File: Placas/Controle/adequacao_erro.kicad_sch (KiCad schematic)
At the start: 5 parts, among them U12 H11L1

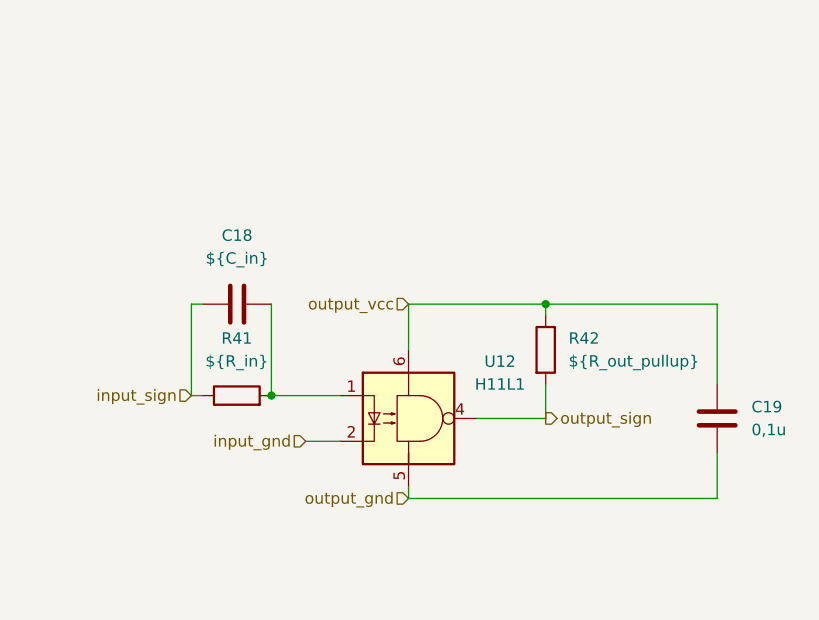
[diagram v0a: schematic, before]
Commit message: Adição de circuitos opcionais para PWM
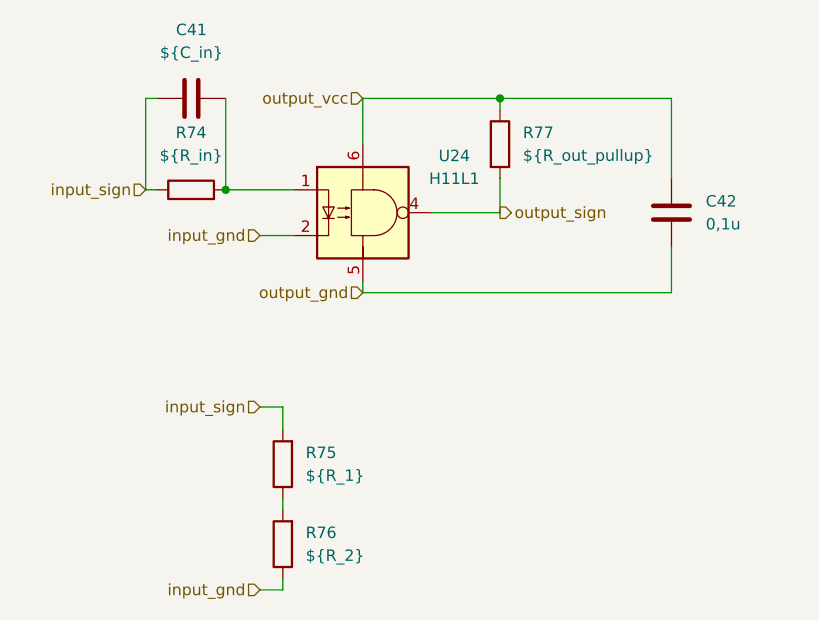
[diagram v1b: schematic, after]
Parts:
- removed C18: ${C_in}, Capacitor_THT:C_Disc_D8.0mm_W5.0mm_P7.50mm, symbol Device:C
- removed C19: 0,1u, Capacitor_THT:C_Disc_D8.0mm_W5.0mm_P7.50mm, symbol Device:C
- removed R41: ${R_in}, Resistor_THT:R_Axial_DIN0207_L6.3mm_D2.5mm_P7.62mm_Horizontal, symbol Device:R
- removed R42: ${R_out_pullup}, Resistor_THT:R_Axial_DIN0207_L6.3mm_D2.5mm_P7.62mm_Horizontal, symbol Device:R
- removed U12: H11L1, Package_DIP:DIP-6_W7.62mm, symbol Isolator:H11L1
- added C41: ${C_in}, Capacitor_THT:C_Disc_D8.0mm_W5.0mm_P7.50mm, symbol Device:C
- added C42: 0,1u, Capacitor_THT:C_Disc_D8.0mm_W5.0mm_P7.50mm, symbol Device:C
- added R74: ${R_in}, Resistor_THT:R_Axial_DIN0207_L6.3mm_D2.5mm_P7.62mm_Horizontal, symbol Device:R
- added R75: ${R_1}, Resistor_THT:R_Axial_DIN0207_L6.3mm_D2.5mm_P7.62mm_Horizontal, symbol Device:R
- added R76: ${R_2}, Resistor_THT:R_Axial_DIN0207_L6.3mm_D2.5mm_P7.62mm_Horizontal, symbol Device:R
- added R77: ${R_out_pullup}, Resistor_THT:R_Axial_DIN0207_L6.3mm_D2.5mm_P7.62mm_Horizontal, symbol Device:R
- added U24: H11L1, Package_DIP:DIP-6_W7.62mm, symbol Isolator:H11L1
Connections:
- net input_gnd: now also R76.1, U24.2
- net input_sign: now also C41.1, R74.1, R75.2
- net output_gnd: now also C42.2, U24.5
- net output_sign: now also R77.2, U24.4
- net output_vcc: now also C42.1, R77.1, U24.6
- new net: R75.1, R76.2
- new net: C41.2, R74.2, U24.1

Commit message: Modificações nas duas placas, adição de furos para montagem, melhora na posição dos micros e conectores para comunicação SPI
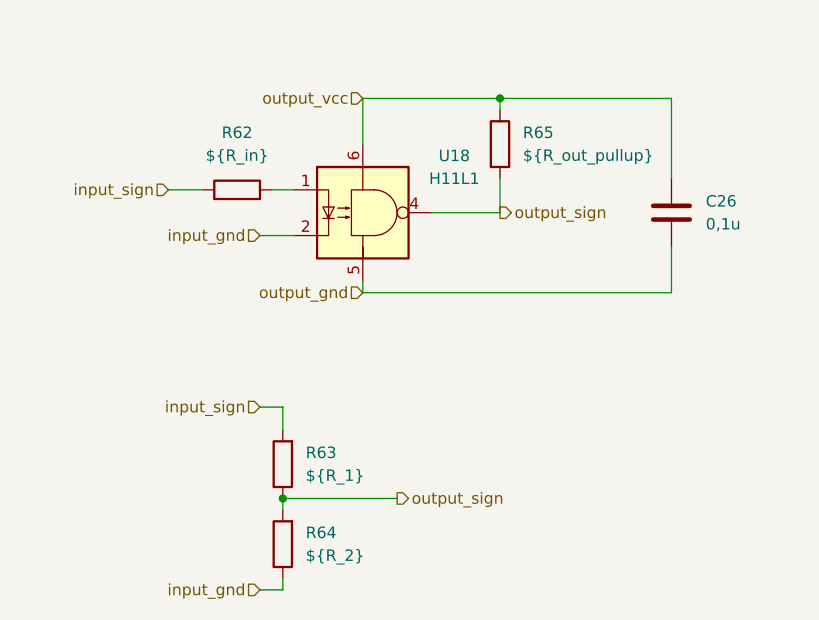
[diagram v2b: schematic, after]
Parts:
- removed C41: ${C_in}, Capacitor_THT:C_Disc_D8.0mm_W5.0mm_P7.50mm, symbol Device:C
- C26: renamed from C42; footprint Capacitor_THT:C_Disc_D8.0mm_W5.0mm_P7.50mm -> Capacitor_SMD:C_0805_2012Metric_Pad1.18x1.45mm_HandSolder
- R62: renamed from R74; footprint Resistor_THT:R_Axial_DIN0207_L6.3mm_D2.5mm_P7.62mm_Horizontal -> Resistor_SMD:R_0805_2012Metric_Pad1.20x1.40mm_HandSolder
- R63: renamed from R75; footprint Resistor_THT:R_Axial_DIN0207_L6.3mm_D2.5mm_P7.62mm_Horizontal -> Resistor_SMD:R_0805_2012Metric_Pad1.20x1.40mm_HandSolder
- R64: renamed from R76; footprint Resistor_THT:R_Axial_DIN0207_L6.3mm_D2.5mm_P7.62mm_Horizontal -> Resistor_SMD:R_0805_2012Metric_Pad1.20x1.40mm_HandSolder
- R65: renamed from R77; footprint Resistor_THT:R_Axial_DIN0207_L6.3mm_D2.5mm_P7.62mm_Horizontal -> Resistor_SMD:R_0805_2012Metric_Pad1.20x1.40mm_HandSolder
- renumbered U24 to U18
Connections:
- net output_sign: now also R63.1, R64.2
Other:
- moved on the sheet: R62

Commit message: Criação dos arquivos em C para o firmware dos dois micros e script em python para salvar aquisição dos dados e envio de comandos
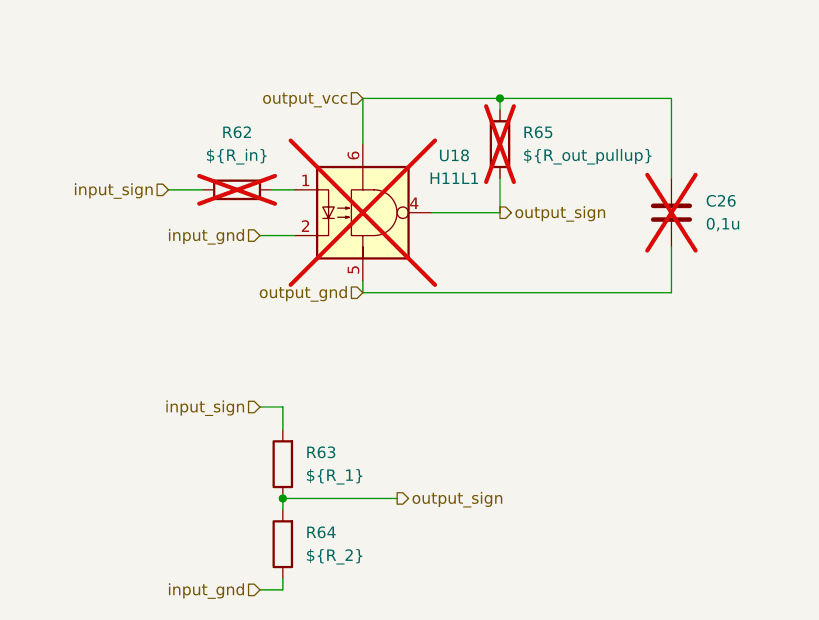
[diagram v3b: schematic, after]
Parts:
- C26, R62, R65, U18: now not fitted
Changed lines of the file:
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@@
 		(in_bom yes)
 		(on_board yes)
-		(dnp no)
+		(dnp yes)
 		(fields_autoplaced yes)
 		(property "Reference" "C26"
@@
 		(in_bom yes)
 		(on_board yes)
-		(dnp no)
+		(dnp yes)
 		(fields_autoplaced yes)
 		(property "Reference" "U18"
@@
 		(in_bom yes)
 		(on_board yes)
-		(dnp no)
+		(dnp yes)
 		(fields_autoplaced yes)
 		(property "Reference" "R65"
@@
 		(in_bom yes)
 		(on_board yes)
-		(dnp no)
+		(dnp yes)
 		(fields_autoplaced yes)
 		(property "Reference" "R62"

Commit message: Mudanças no firmware e calibração da tensão de entrada e saída
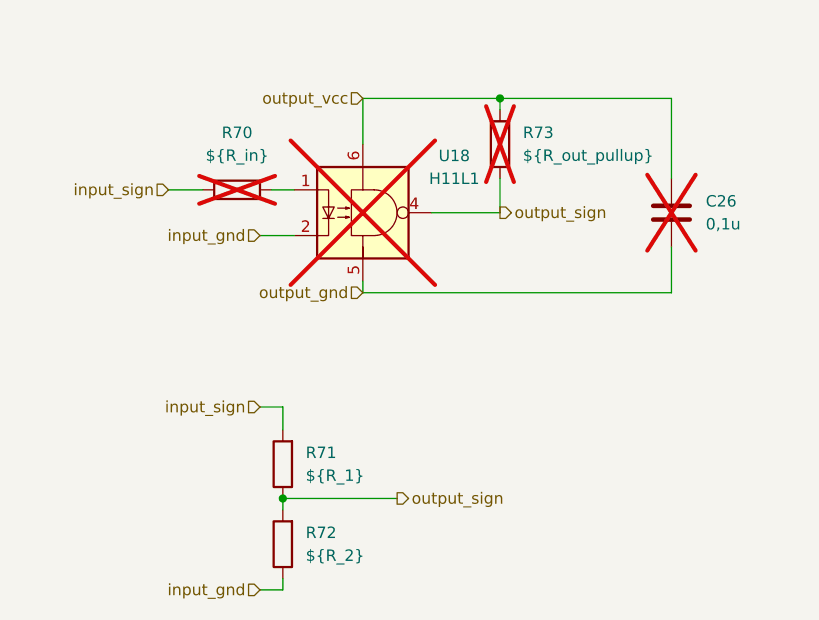
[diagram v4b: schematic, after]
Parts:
- renumbered R62 to R70, R63 to R71, R64 to R72, R65 to R73
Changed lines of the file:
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@@
 		(dnp no)
 		(fields_autoplaced yes)
-		(property "Reference" "R64"
+		(property "Reference" "R72"
 			(at 91.44 102.8699 0)
 			(effects
@@
 			(project "Controle"
 				(path "/01568b53-f202-4f02-9c1a-9c10c7610b4b/4badf859-7634-4899-8760-3495612f97fd/85640af9-3c56-4a5e-9eff-4e92d4f132b9/84d61ec8-e9e5-4da4-b009-e86fb4fe152b"
-					(reference "R64")
-					(unit 1)
-				)
-				(path "/01568b53-f202-4f02-9c1a-9c10c7610b4b/4badf859-7634-4899-8760-3495612f97fd/8dc5e02a-820d-46fa-a29a-1b06a2e85f06/84d61ec8-e9e5-4da4-b009-e86fb4fe152b"
-					(reference "R50")
-					(unit 1)
-				)
-				(path "/01568b53-f202-4f02-9c1a-9c10c7610b4b/4badf859-7634-4899-8760-3495612f97fd/8e1b14a0-5a44-45bc-9dce-fdb022fd1001/84d61ec8-e9e5-4da4-b009-e86fb4fe152b"
-					(reference "R78")
+					(reference "R72")
+					(unit 1)
+				)
+				(path "/01568b53-f202-4f02-9c1a-9c10c7610b4b/4badf859-7634-4899-8760-3495612f97fd/8dc5e02a-820d-46fa-a29a-1b06a2e85f06/84d61ec8-e9e5-4da4-b009-e86fb4fe152b"
+					(reference "R58")
+					(unit 1)
+				)
+				(path "/01568b53-f202-4f02-9c1a-9c10c7610b4b/4badf859-7634-4899-8760-3495612f97fd/8e1b14a0-5a44-45bc-9dce-fdb022fd1001/84d61ec8-e9e5-4da4-b009-e86fb4fe152b"
+					(reference "R86")
 					(unit 1)
 				)
@@
 		(dnp no)
 		(fields_autoplaced yes)
-		(property "Reference" "R63"
+		(property "Reference" "R71"
 			(at 91.44 93.9799 0)
 			(effects
@@
 			(project "Controle"
 				(path "/01568b53-f202-4f02-9c1a-9c10c7610b4b/4badf859-7634-4899-8760-3495612f97fd/85640af9-3c56-4a5e-9eff-4e92d4f132b9/84d61ec8-e9e5-4da4-b009-e86fb4fe152b"
-					(reference "R63")
-					(unit 1)
-				)
-				(path "/01568b53-f202-4f02-9c1a-9c10c7610b4b/4badf859-7634-4899-8760-3495612f97fd/8dc5e02a-820d-46fa-a29a-1b06a2e85f06/84d61ec8-e9e5-4da4-b009-e86fb4fe152b"
-					(reference "R49")
-					(unit 1)
-				)
-				(path "/01568b53-f202-4f02-9c1a-9c10c7610b4b/4badf859-7634-4899-8760-3495612f97fd/8e1b14a0-5a44-45bc-9dce-fdb022fd1001/84d61ec8-e9e5-4da4-b009-e86fb4fe152b"
-					(reference "R77")
+					(reference "R71")
+					(unit 1)
+				)
+				(path "/01568b53-f202-4f02-9c1a-9c10c7610b4b/4badf859-7634-4899-8760-3495612f97fd/8dc5e02a-820d-46fa-a29a-1b06a2e85f06/84d61ec8-e9e5-4da4-b009-e86fb4fe152b"
+					(reference "R57")
+					(unit 1)
+				)
+				(path "/01568b53-f202-4f02-9c1a-9c10c7610b4b/4badf859-7634-4899-8760-3495612f97fd/8e1b14a0-5a44-45bc-9dce-fdb022fd1001/84d61ec8-e9e5-4da4-b009-e86fb4fe152b"
+					(reference "R85")
 					(unit 1)
 				)
@@
 		(dnp yes)
 		(fields_autoplaced yes)
-		(property "Reference" "R65"
+		(property "Reference" "R73"
 			(at 115.57 58.4199 0)
 			(effects
@@
 			(project "Controle"
 				(path "/01568b53-f202-4f02-9c1a-9c10c7610b4b/4badf859-7634-4899-8760-3495612f97fd/85640af9-3c56-4a5e-9eff-4e92d4f132b9/84d61ec8-e9e5-4da4-b009-e86fb4fe152b"
-					(reference "R65")
-					(unit 1)
-				)
-				(path "/01568b53-f202-4f02-9c1a-9c10c7610b4b/4badf859-7634-4899-8760-3495612f97fd/8dc5e02a-820d-46fa-a29a-1b06a2e85f06/84d61ec8-e9e5-4da4-b009-e86fb4fe152b"
-					(reference "R51")
-					(unit 1)
-				)
-				(path "/01568b53-f202-4f02-9c1a-9c10c7610b4b/4badf859-7634-4899-8760-3495612f97fd/8e1b14a0-5a44-45bc-9dce-fdb022fd1001/84d61ec8-e9e5-4da4-b009-e86fb4fe152b"
-					(reference "R79")
+					(reference "R73")
+					(unit 1)
+				)
+				(path "/01568b53-f202-4f02-9c1a-9c10c7610b4b/4badf859-7634-4899-8760-3495612f97fd/8dc5e02a-820d-46fa-a29a-1b06a2e85f06/84d61ec8-e9e5-4da4-b009-e86fb4fe152b"
+					(reference "R59")
+					(unit 1)
+				)
+				(path "/01568b53-f202-4f02-9c1a-9c10c7610b4b/4badf859-7634-4899-8760-3495612f97fd/8e1b14a0-5a44-45bc-9dce-fdb022fd1001/84d61ec8-e9e5-4da4-b009-e86fb4fe152b"
+					(reference "R87")
 					(unit 1)
 				)
@@
 		(dnp yes)
 		(fields_autoplaced yes)
-		(property "Reference" "R62"
+		(property "Reference" "R70"
 			(at 83.82 58.42 90)
 			(effects
@@
 			(project "Controle"
 				(path "/01568b53-f202-4f02-9c1a-9c10c7610b4b/4badf859-7634-4899-8760-3495612f97fd/85640af9-3c56-4a5e-9eff-4e92d4f132b9/84d61ec8-e9e5-4da4-b009-e86fb4fe152b"
-					(reference "R62")
-					(unit 1)
-				)
-				(path "/01568b53-f202-4f02-9c1a-9c10c7610b4b/4badf859-7634-4899-8760-3495612f97fd/8dc5e02a-820d-46fa-a29a-1b06a2e85f06/84d61ec8-e9e5-4da4-b009-e86fb4fe152b"
-					(reference "R48")
-					(unit 1)
-				)
-				(path "/01568b53-f202-4f02-9c1a-9c10c7610b4b/4badf859-7634-4899-8760-3495612f97fd/8e1b14a0-5a44-45bc-9dce-fdb022fd1001/84d61ec8-e9e5-4da4-b009-e86fb4fe152b"
-					(reference "R76")
-					(unit 1)
-				)
+					(reference "R70")
+					(unit 1)
+				)
+				(path "/01568b53-f202-4f02-9c1a-9c10c7610b4b/4badf859-7634-4899-8760-3495612f97fd/8dc5e02a-820d-46fa-a29a-1b06a2e85f06/84d61ec8-e9e5-4da4-b009-e86fb4fe152b"
+					(reference "R56")
+					(unit 1)
+				)
+				(path "/01568b53-f202-4f02-9c1a-9c10c7610b4b/4badf859-7634-4899-8760-3495612f97fd/8e1b14a0-5a44-45bc-9dce-fdb022fd1001/84d61ec8-e9e5-4da4-b009-e86fb4fe152b"
+					(reference "R84")
+					(unit 1)
+				)
